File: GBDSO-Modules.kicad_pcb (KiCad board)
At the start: 2 copper layers, 136.5 x 24.6 mm, 84 parts, among them J1 MJ-3523-SMT-TR, J10 Conn_01x10, J11 Conn_01x10, J12 Conn_01x12, J13 Conn_01x16, J14 Conn_01x12, J15 Conn_01x10, J16 Conn_01x28, J17 Conn_01x32, J18 Conn_01x06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

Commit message: C8 on the dig pot wasn't connected correctly
changed the schematic, updated the netlist and PCB
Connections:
- C8 pad 2: -5V -> GND

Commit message: fixed schematic and updated PCB
Fixed the schematic after having found the issues in the GBDSO schematic (which is also fixed on the repo).
Continued making the PCB for the modules. We're not at 7 modules from 10.
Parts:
- J13: footprint Package_DIP:DIP-16_W7.62mm -> Package_DIP:DIP-24_W15.24mm
- J14: footprint Package_DIP:DIP-12_W7.62mm -> Package_DIP:DIP-12_W10.16mm_LongPads
- J19: footprint Package_DIP:DIP-6_W7.62mm -> Package_DIP:DIP-6_W10.16mm
- moved C20 203.5 mm to (71.3, 111.2), turned to 90 degrees
- moved C19 190.9 mm to (81.6, 117.6), turned to 90 degrees
- moved U8 189.9 mm to (78.6, 112.9)
- moved D3 189.8 mm to (77.6, 117.6), turned to 180 degrees
- moved R17 188.5 mm to (86.0, 111.1), turned to 270 degrees
- moved C21 187.9 mm to (71.3, 114.7), turned to 90 degrees
- moved R16 186.6 mm to (86.0, 114.7), turned to 270 degrees
- moved J19 181.4 mm to (73.5, 110.4)
- moved R15 177.4 mm to (76.8, 109.1)
- moved U5 155.4 mm to (120.1, 110.7)
- moved C17 153.8 mm to (157.4, 120.1), turned to 270 degrees
- moved U4 151.1 mm to (162.4, 132.7)
- moved C29 150.2 mm to (118.7, 104.4)
- moved J14 146.6 mm to (115.0, 104.3)
- moved J13 138.6 mm to (154.6, 118.9)
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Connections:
- SW1 pad 3: Net-(SW1-Pad3) -> GND
- SW2 pad 3: Net-(SW2-Pad3) -> GND
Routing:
- net D4: track 0.00 -> 35.2 mm, vias 0 -> 4
- net +2.5V: track 61.1 -> 94.7 mm, vias 4 -> 6
- net ADC_IN2: track 14.7 -> 47.3 mm, vias 0 -> 2
- net D7: track 0.00 -> 32.5 mm, vias 0 -> 2
- net ~ADC_PWRDN: track 0.00 -> 29.0 mm, vias 0 -> 2
- net +5VC: track 7.14 -> 33.5 mm
- net ADC_SEL: track 0.00 -> 26.2 mm
- net D6: track 0.00 -> 25.1 mm, vias 0 -> 2
- net D5: track 0.00 -> 24.0 mm, vias 0 -> 2
- net ADC_IN1: track 14.7 -> 37.7 mm, vias 0 -> 2
- net ADC_EN: track 9.45 -> 31.9 mm, vias 0 -> 2
- net GND: track 55.4 -> 73.8 mm, vias 20 -> 31
- net Net-(C19-Pad1): track 0.00 -> 14.3 mm
- net +5V: track 45.3 -> 55.1 mm
- net D0: track 0.00 -> 9.43 mm
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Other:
- board size 136.5 x 24.6 mm -> 147.3 x 60.7 mm

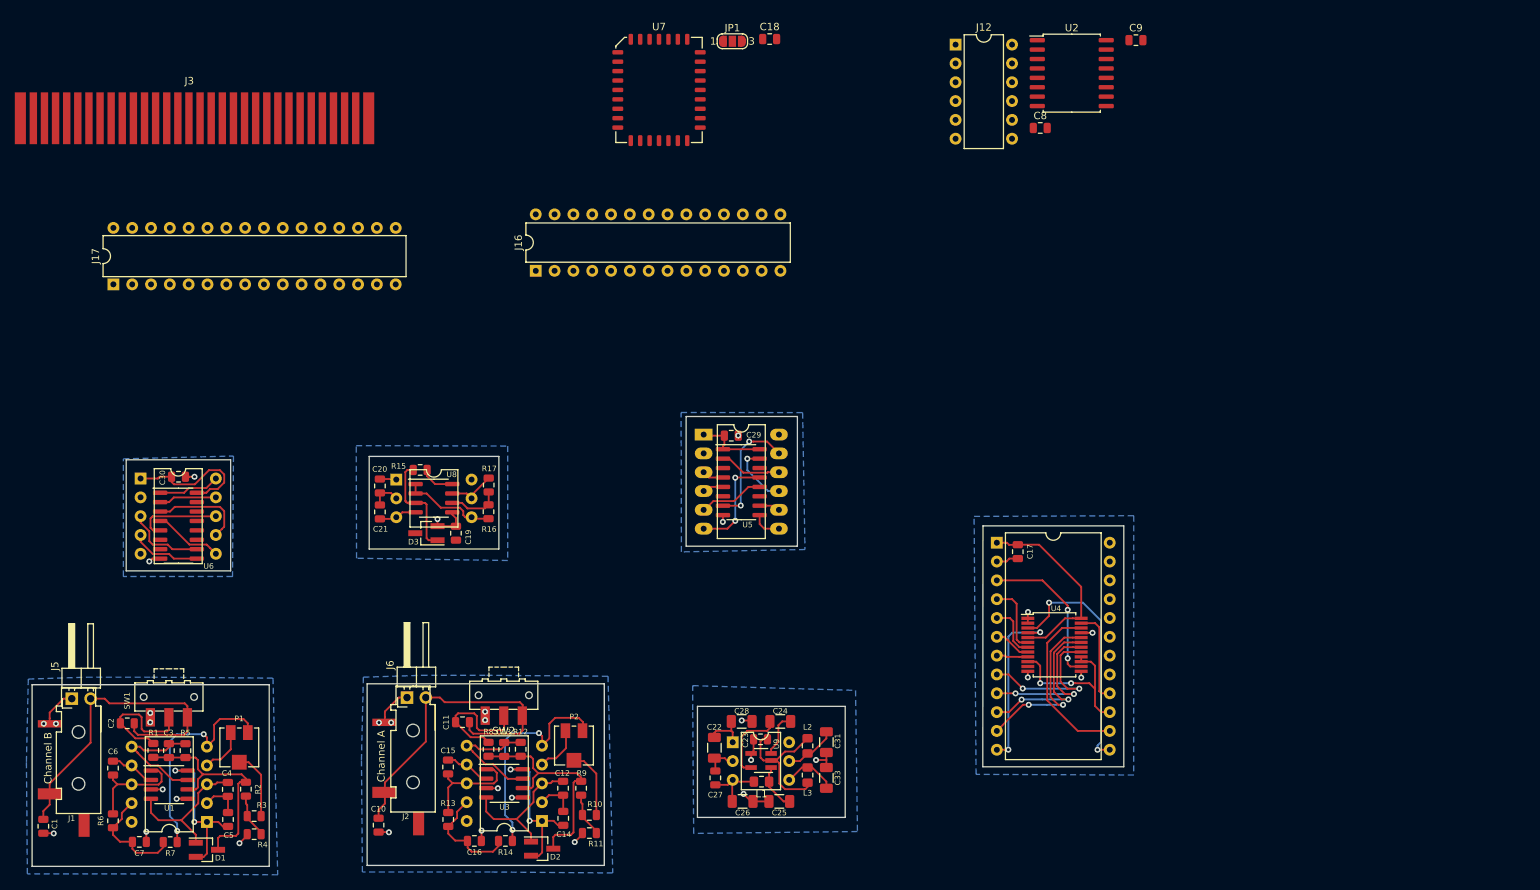
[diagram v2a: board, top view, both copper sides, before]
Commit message: Finished and panelized the PCBs, except for edge connector; too big
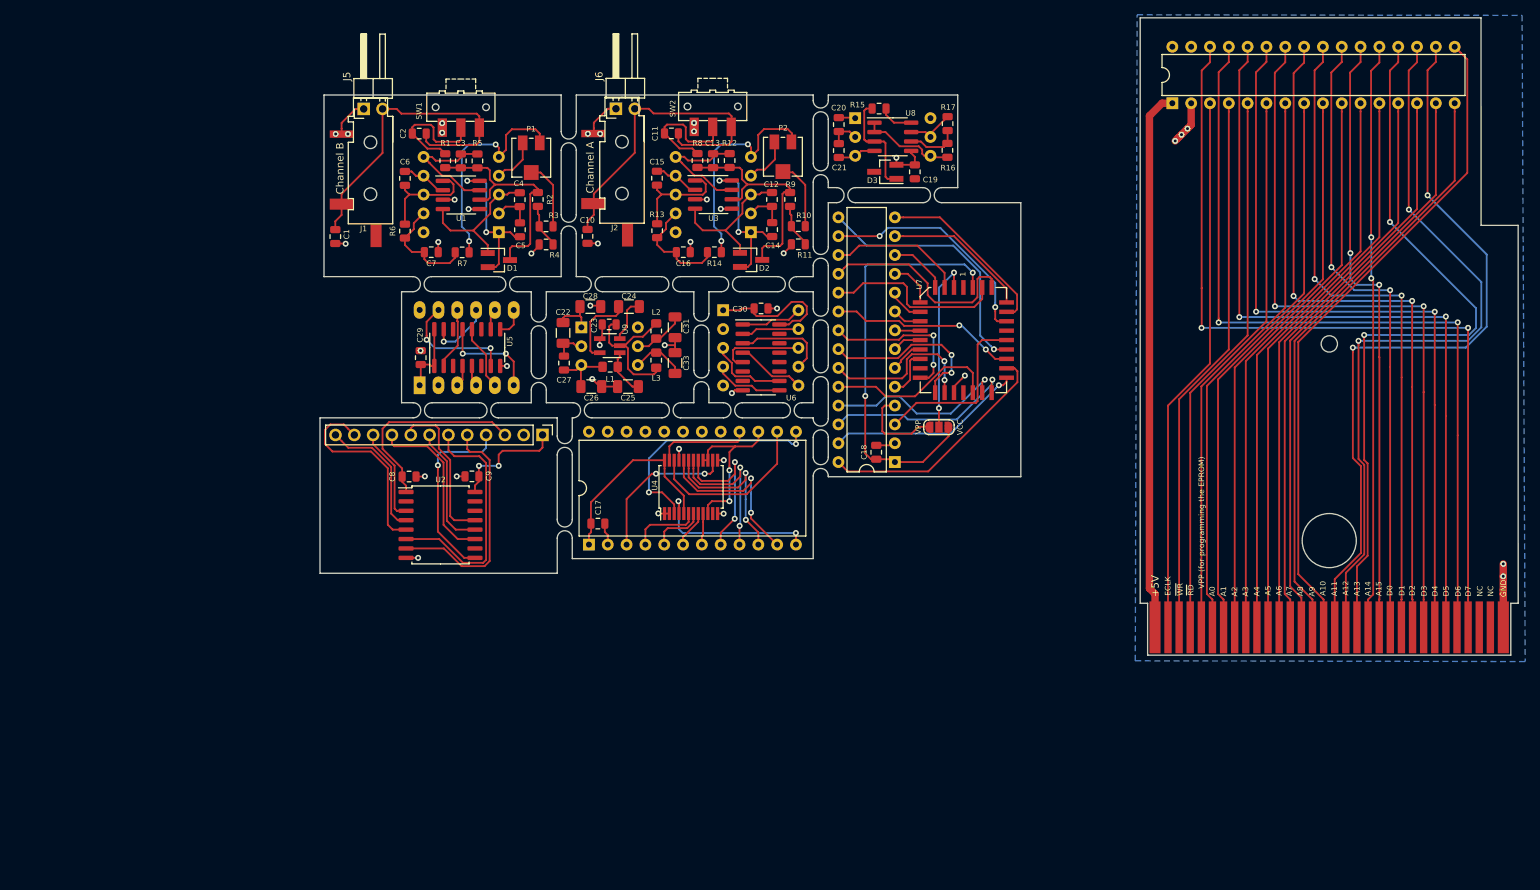
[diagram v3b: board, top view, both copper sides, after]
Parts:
- added REF**: OSHW-Logo2_7.3x6mm_SilkScreen, Symbol:OSHW-Logo2_7.3x6mm_SilkScreen, B.Cu at (104.2, 79.5)
- added REF**: OSHW-Logo2_7.3x6mm_SilkScreen, Symbol:OSHW-Logo2_7.3x6mm_SilkScreen, B.Cu at (199.5, 109.3)
- added REF**: OSHW-Logo2_7.3x6mm_SilkScreen, Symbol:OSHW-Logo2_7.3x6mm_SilkScreen, B.Cu at (70.2, 79.6)
- added REF**: OSHW-Logo2_7.3x6mm_SilkScreen, Symbol:OSHW-Logo2_7.3x6mm_SilkScreen, B.Cu at (122.7, 94.7)
- added REF**: OSHW-Logo2_7.3x6mm_SilkScreen, Symbol:OSHW-Logo2_7.3x6mm_SilkScreen, B.Cu at (102.2, 91.4)
- added REF**: OSHW-Logo2_7.3x6mm_SilkScreen, Symbol:OSHW-Logo2_7.3x6mm_SilkScreen, B.Cu at (67.7, 118.3)
- added REF**: OSHW-Logo2_7.3x6mm_SilkScreen, Symbol:OSHW-Logo2_7.3x6mm_SilkScreen, B.Cu at (125.7, 111.5)
- added REF**: OSHW-Logo2_7.3x6mm_SilkScreen, Symbol:OSHW-Logo2_7.3x6mm_SilkScreen, B.Cu at (153.4, 106.3)
- added REF**: OSHW-Logo2_7.3x6mm_SilkScreen, Symbol:OSHW-Logo2_7.3x6mm_SilkScreen, B.Cu at (83.0, 92.5)
- added REF**: OSHW-Logo2_7.3x6mm_SilkScreen, Symbol:OSHW-Logo2_7.3x6mm_SilkScreen, B.Cu at (140.6, 63.5)
- J12: footprint Package_DIP:DIP-12_W7.62mm -> Connector_PinHeader_2.54mm:PinHeader_1x12_P2.54mm_Vertical
- U7: footprint Package_LCC:PLCC-32_11.4x14.0mm_P1.27mm -> PLCC32_HandSolder:PLCC-32_HandSolder
- moved J3 167.8 mm to (198.7, 130.3)
- moved J17 145.0 mm to (178.3, 59.6)
- moved C9 107.2 mm to (83.7, 109.9), turned to 180 degrees
- moved U2 104.8 mm to (79.5, 116.5)
- moved C8 97.3 mm to (75.3, 110.0)
- moved C2 88.8 mm to (76.6, 63.7)
- moved C4 88.8 mm to (90.2, 72.6)
- moved C6 88.8 mm to (74.7, 69.7)
- moved C7 88.8 mm to (78.3, 79.7)
- moved D1 88.8 mm to (87.4, 80.7)
- moved J1 88.8 mm to (70.1, 68.2)
- moved J10 88.8 mm to (87.4, 77.0)
- moved P1 88.8 mm to (91.7, 66.9)
- moved R1 88.8 mm to (80.1, 67.3)
- moved R3 88.8 mm to (93.8, 76.2)
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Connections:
- C8 pad 1: Net-(C8-Pad1) -> -5V
- J12 pad 10: DPOT_0H -> DPOT_1H
- U2 pad 1: Net-(C8-Pad1) -> -5V
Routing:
- net D7: track 32.5 -> 180.0 mm, vias 2 -> 4
- net D1: track 7.36 -> 145.6 mm, vias 0 -> 5
- net D6: track 25.1 -> 163.0 mm, vias 2 -> 5
- net D5: track 24.0 -> 156.7 mm, vias 2 -> 5
- net A11: track 0.00 -> 131.7 mm, vias 0 -> 4
- net +5V: track 55.1 -> 184.9 mm, vias 0 -> 2
- net D4: track 35.2 -> 163.3 mm, vias 4 -> 7
- net A13: track 12.8 -> 140.5 mm, vias 0 -> 2
- net A10: track 0.00 -> 125.0 mm, vias 0 -> 1
- net D3: track 4.25 -> 126.3 mm, vias 0 -> 2
- net A12: track 0.00 -> 118.3 mm, vias 0 -> 2
- net D2: track 5.04 -> 121.4 mm, vias 0 -> 4
- net A15: track 0.00 -> 107.8 mm, vias 0 -> 4
- net D0: track 9.43 -> 115.0 mm, vias 0 -> 4
- net A9: track 0.00 -> 105.3 mm
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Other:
- board size 147.3 x 60.7 mm -> 161.7 x 86 mm
- board text added: "+/- 2.5V Gen"
- board text added: "+5V"
- board text added: "1"
- board text added: "A0"
- board text added: "A1"
- board text added: "A10"
- board text added: "A11"
- board text added: "A12"
- board text added: "A13"
- board text added: "A14"
- board text added: "A15"
- board text added: "A2"
- board text added: "A3"
- board text added: "A4"
- board text added: "A5"
- board text added: "A6"
- board text added: "A7"
- board text added: "A8"
- board text added: "A9"
- board text added: "ADC"
- board text added: "D0"
- board text added: "D1"
- board text added: "D2"
- board text added: "D3"
- board text added: "D4"
- board text added: "D5"
- board text added: "D6"
- board text added: "D7"
- board text added: "DFF"
- board text added: "Demux"
- board text added: "Digital Pot"
- board text added: "ECLK"
- board text added: "Edge Connector"
- board text added: "GND"
- board text added: "NC"
- board text added: "ROM"
- board text added: "VPP (for programming the EPROM)"
- board text added: "Voltage Inverter"
- board text added: "~RD"
- board text added: "~WR"

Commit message: forgot to add the ground plane on the panel, fixed
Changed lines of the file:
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@@
   )
   (setup
-    (last_trace_width 0.5)
+    (last_trace_width 0.25)
     (user_trace_width 0.5)
     (user_trace_width 0.75)
@@
       )
     )
+  )
+  (zone (net 1) (net_name GND) (layer B.Cu) (hatch edge 0.508)
+    (connect_pads (clearance 0.508))
+    (min_thickness 0.254)
+    (fill yes (arc_segments 32) (thermal_gap 0.508) (thermal_bridge_width 0.508))
+    (polygon
+      (pts
+        (xy 159.131 123.9012) (xy 62.5094 123.8504) (xy 62.8904 57.6326) (xy 159.131 57.6326)
+      )
+    )
